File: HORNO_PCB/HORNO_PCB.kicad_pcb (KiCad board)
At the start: 2 copper layers, 198 x 218 mm, 115 parts, among them J0_1 Alimentacion dispositivo seri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, J0_10 Terminales de tornillo espaci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, J0_11 Terminales de tornillo espaci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, J0_12 Terminales de tornillo espaci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, J0_13 Terminales de tornillo espaci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, J0_14 Terminales de tornillo espaci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, J0_15 Terminales de tornillo espaci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, J0_18 Terminales de tornillo espaci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, J0_2 Terminales de tornillo espaci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, J0_3 Terminales de tornillo espaci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, J0_4 Terminales de tornillo espaci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, J0_5 Terminales de tornillo espaci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, J0_6 Terminales de tornillo espaci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, J0_7 Terminales de tornillo espaci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, J0_8 Terminales de tornillo espaci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, J0_9 Terminales de tornillo espaci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, J1 +5V +24V, J10 switch, J11 switch, J12 switch, J13 switch, J14 switch, J15 switch, J16 switch, J17 switch, J18 switch, J19 switch, J20 switch, J21 switch, J22 switch, J23 switch, J24 Screw_Terminal_01x20, J25 Screw_Terminal_01x20, J26 Screw_Terminal_01x20, J27 Screw_Terminal_01x20, J7 24VDC, J8 switch, J9 switch, K1 Relay 1, K2 Relay 2, K6 Relay 4, K7 Relay 3, K8 Relay 2, K9 Relay 1, Q1 2N2222, Q2 2N2222, Q6 IRG4PF50W, Q7 IRG4PF50W, U1 TLP521-1, U10 LM741, U15 TLP250, U17 LM741, U18 LM741, U19 TLP250, U2 TLP521-1, U25 UDN2981A, U3 TLP521-1, U4 TLP521-1, U9 LM741

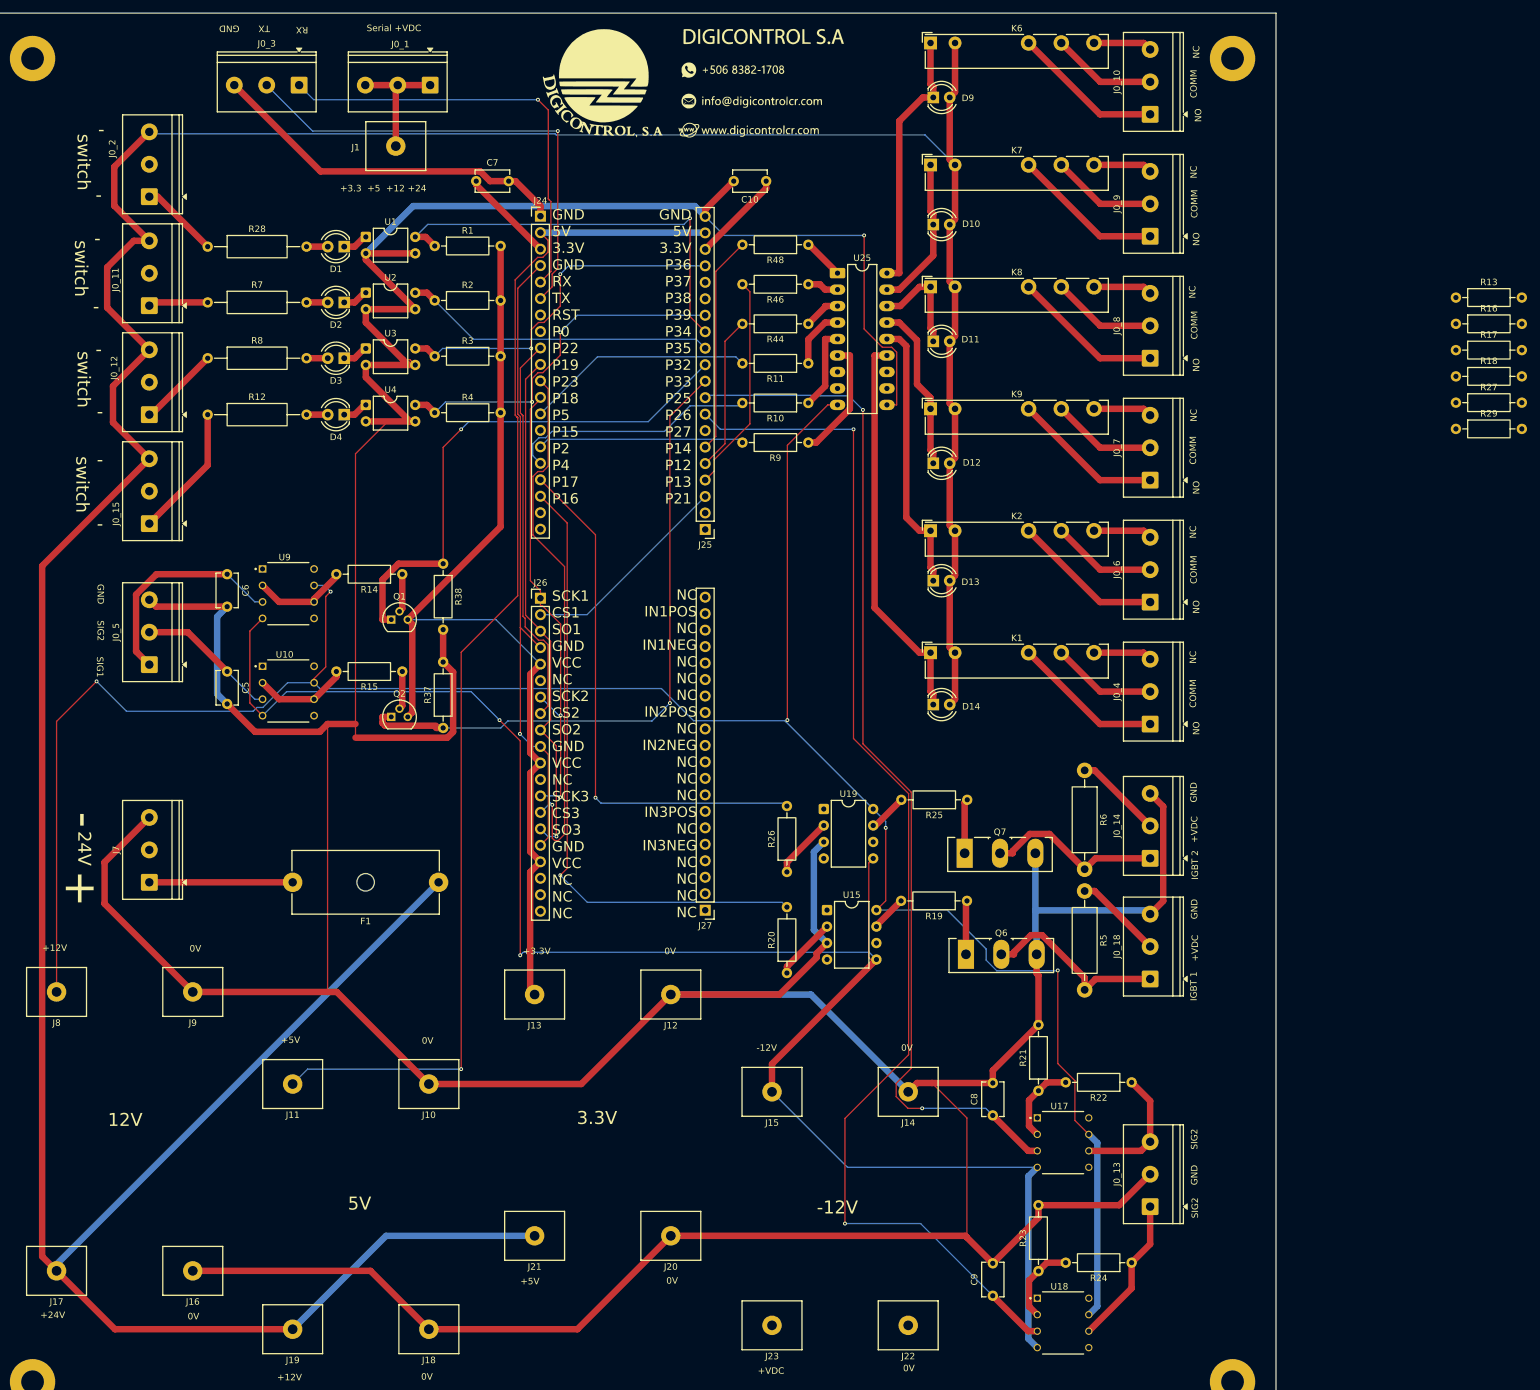
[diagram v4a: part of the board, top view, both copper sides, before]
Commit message: Correccion de esquematico y PCB
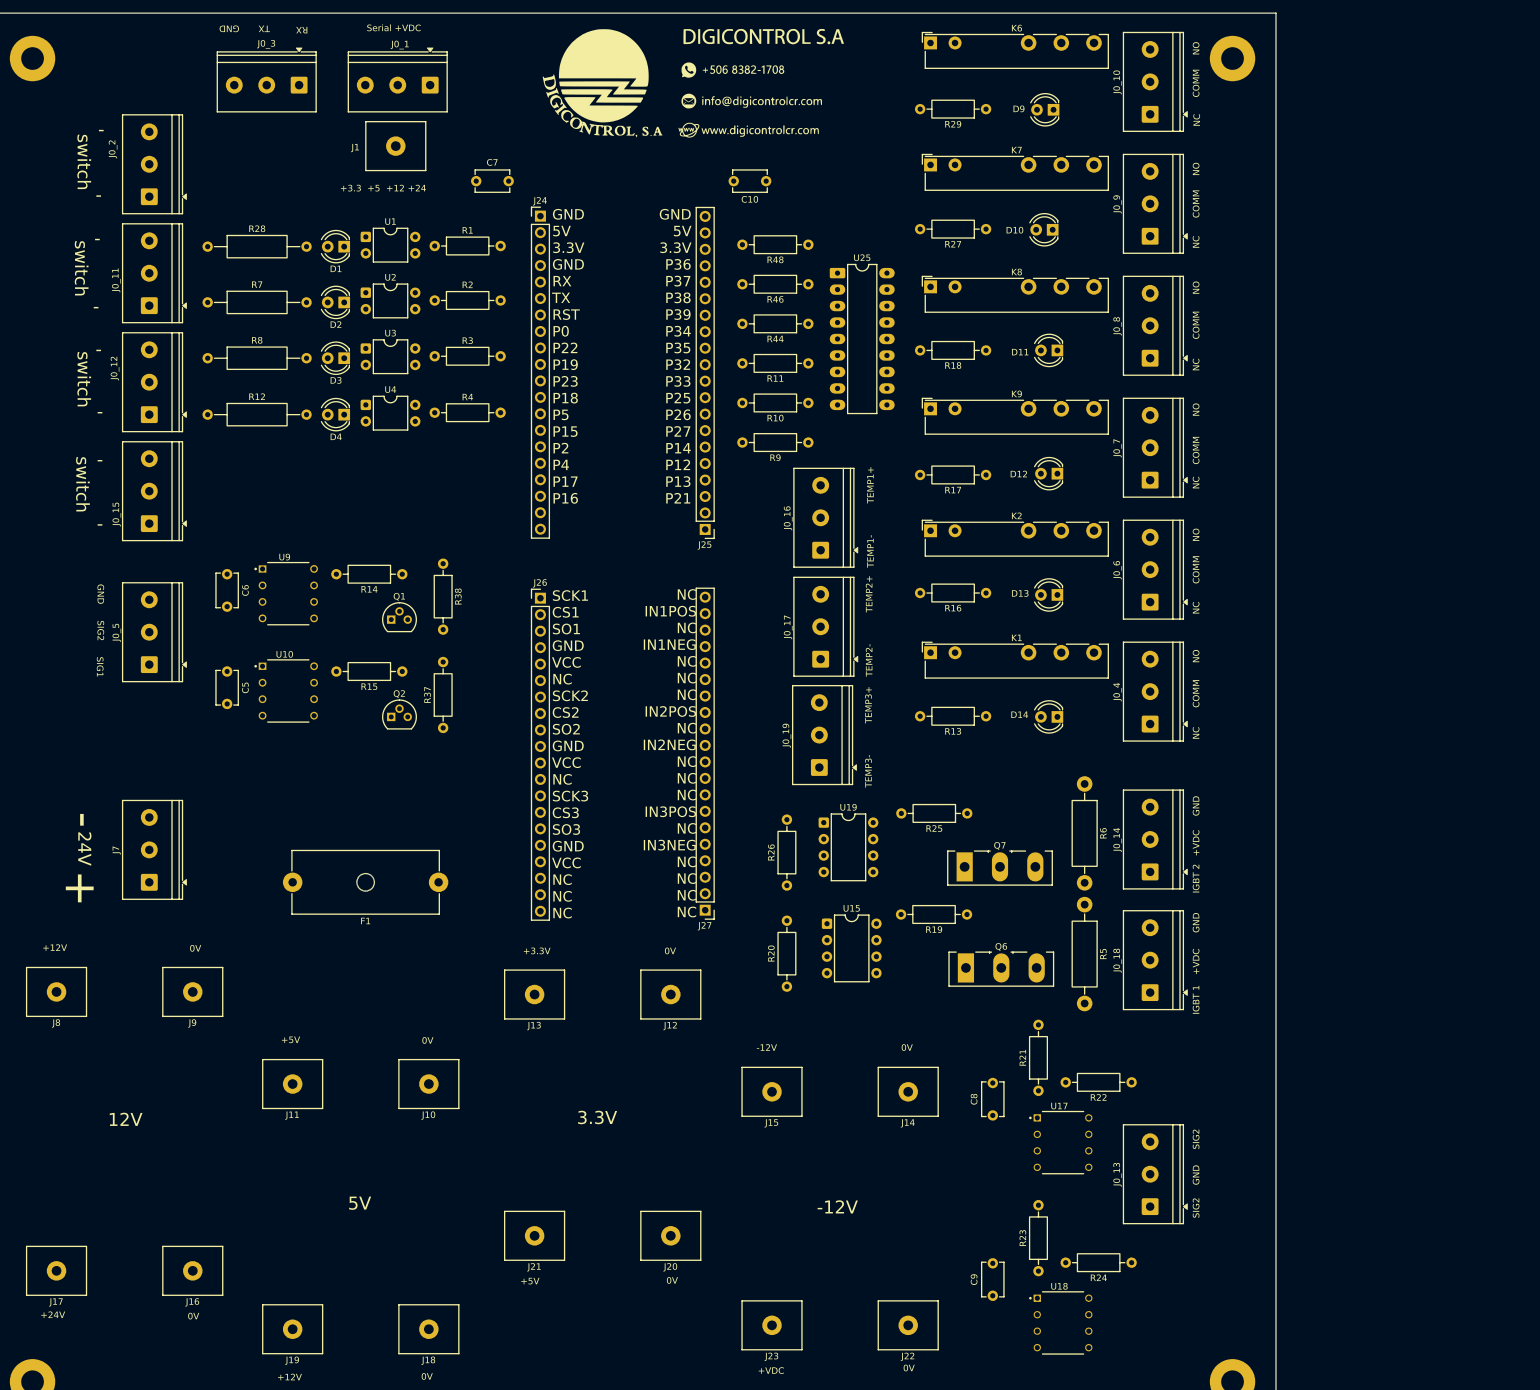
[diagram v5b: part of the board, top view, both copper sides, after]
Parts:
- added J0_16: Terminales de tornillo espaciados en 5mm, TerminalBlock_Phoenix:TerminalBlock_Phoenix_PT-1,5-3-5.0-H_1x03_P5.00mm_Horizontal, F.Cu at (429.5, 249.8)
- added J0_17: Terminales de tornillo espaciados en 5mm, TerminalBlock_Phoenix:TerminalBlock_Phoenix_PT-1,5-3-5.0-H_1x03_P5.00mm_Horizontal, F.Cu at (429.5, 266.6)
- added J0_19: Terminales de tornillo espaciados en 5mm, TerminalBlock_Phoenix:TerminalBlock_Phoenix_PT-1,5-3-5.0-H_1x03_P5.00mm_Horizontal, F.Cu at (429.3, 283.3)
- moved R13 97.0 mm to (455.0, 275.4), turned to 180 degrees
- moved R29 87.6 mm to (455.0, 181.8), turned to 180 degrees
- moved R16 83.5 mm to (455.0, 256.4), turned to 180 degrees
- moved R27 77.2 mm to (455.0, 200.3), turned to 180 degrees
- moved R17 75.0 mm to (455.0, 238.2), turned to 180 degrees
- moved R18 72.6 mm to (455.0, 219.0), turned to 180 degrees
- moved D13 19.3 mm to (466.0, 256.7), turned to 180 degrees
- moved D14 19.2 mm to (466.0, 275.5), turned to 180 degrees
- moved D12 19.2 mm to (466.0, 238.0), turned to 180 degrees
- moved D11 19.2 mm to (466.0, 219.0), turned to 180 degrees
- moved D9 18.6 mm to (465.4, 181.9), turned to 180 degrees
- moved D10 18.4 mm to (465.3, 200.4), turned to 180 degrees
- moved J0_18 2.10 mm to (480.3, 318.0)
- moved Q7 2.10 mm to (451.7, 298.6)
- moved R25 2.10 mm to (452.1, 290.4)
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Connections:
- J27 pad 11: unconnected-(J27-Pin_11-Pad11) -> Net-(J0_17-Pin_1)
- J27 pad 13: unconnected-(J27-Pin_13-Pad13) -> Net-(J0_17-Pin_3)
- J27 pad 17: unconnected-(J27-Pin_17-Pad17) -> Net-(J0_16-Pin_1)
- J27 pad 19: unconnected-(J27-Pin_19-Pad19) -> Net-(J0_16-Pin_3)
- J27 pad 5: unconnected-(J27-Pin_5-Pad5) -> Net-(J0_19-Pin_1)
- J27 pad 7: unconnected-(J27-Pin_7-Pad7) -> Net-(J0_19-Pin_3)
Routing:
- net Net-(D10-K): track 1061.4 -> 0.00 mm, vias 1 -> 0
- net Net-(D10-A): track 599.0 -> 0.00 mm
- net Net-(J8-Pin_1): track 359.0 -> 0.00 mm, vias 5 -> 0
- net Net-(J15-Pin_1): track 268.0 -> 0.00 mm, vias 2 -> 0
- net Net-(J25-Pin_8): track 190.4 -> 0.00 mm, vias 2 -> 0
- net Net-(J11-Pin_1): track 188.4 -> 0.00 mm, vias 1 -> 0
- net Net-(J25-Pin_9): track 160.5 -> 0.00 mm, vias 2 -> 0
- net Net-(J13-Pin_1): track 156.9 -> 0.00 mm
- net Net-(J25-Pin_10): track 100.6 -> 0.00 mm, vias 1 -> 0
- net Net-(J24-Pin_4): track 98.4 -> 0.00 mm, vias 1 -> 0
- net Net-(J24-Pin_18): track 97.6 -> 0.00 mm, vias 1 -> 0
- net Net-(J24-Pin_11): track 84.0 -> 0.00 mm, vias 1 -> 0
- net Net-(J24-Pin_17): track 82.6 -> 0.00 mm, vias 1 -> 0
- net Net-(J25-Pin_11): track 81.5 -> 0.00 mm, vias 1 -> 0
- net Net-(J24-Pin_10): track 79.9 -> 0.00 mm, vias 1 -> 0
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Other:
- board text added: "TEMP1+"
- board text added: "TEMP1-"
- board text added: "TEMP2+"
- board text added: "TEMP2-"
- board text added: "TEMP3+"
- board text added: "TEMP3-"

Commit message: PCB corregida
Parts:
- removed J10, J11, J12, J13, J14, J15, J16, J17, J18, J19, J20, J21, J22, J23, J8, J9: switch, TerminalBlock_MetzConnect:TerminalBlock_MetzConnect_360271_1x01_Horizontal_ScrewM3.0_Boxed
- removed K6: Relay 4, Relay_THT:Relay_SPDT_Fujitsu_FTR-LYCA005x_FormC_Vertical
- added Fuente_1: 12VDC, Fuente_step:step_source, F.Cu at (323.7, 340.0)
- added Fuente_2: 5VDC, Fuente_step:step_source, F.Cu at (360.2, 353.0)
- added Fuente_3: 3.3VDC, Fuente_step:step_source, F.Cu at (397.6, 340.0)
- added Fuente_4: -12VDC, Fuente_step:step_source, F.Cu at (436.5, 353.0)
- moved C8 7.87 mm to (455.7, 344.8)
- moved C9 6.80 mm to (456.0, 371.5)
- moved R21 6.00 mm to (458.1, 336.5)
- moved U15 5.62 mm to (430.5, 313.0)
- moved R23 5.48 mm to (458.1, 363.2)
- moved R20 5.42 mm to (424.3, 322.5)
- moved R19 5.04 mm to (452.1, 311.0)
- moved Q6 3.80 mm to (451.9, 318.0)
- moved J0_14 2.40 mm to (480.3, 297.0)
- moved R5 2.06 mm to (470.2, 306.5)
- moved Q7 1.62 mm to (451.7, 297.0)
- moved R22 1.16 mm to (477.4, 333.0)
- moved U17 1.06 mm to (466.8, 342.2)
- moved J0_13 1.00 mm to (480.3, 352.0)
- moved R25 0.38 mm to (452.1, 290.0)
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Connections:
- J0_10 pad 2: Net-(J0_10-Pin_2) -> unconnected-(J0_10-Pin_2-Pad2)
- J0_10 pad 3: Net-(J0_10-Pin_3) -> Net-(D10-K)
- R29 pad 2: Net-(U25-O1) -> Net-(J0_10-Pin_1)
- R48 pad 1: Net-(U25-I1) -> Net-(J0_10-Pin_1)
- U25 pad 1: Net-(U25-I1) -> unconnected-(U25-I1-Pad1)
- U25 pad 18: Net-(U25-O1) -> unconnected-(U25-O1-Pad18)
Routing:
- net Net-(D10-K): track 0.00 -> 1046.3 mm
- net Net-(Fuente_1-OUT+): track 0.00 -> 364.9 mm, vias 0 -> 5
- net Net-(Fuente_1-IN+): track 0.00 -> 326.0 mm
- net Net-(Fuente_4-OUT+): track 0.00 -> 232.0 mm, vias 0 -> 1
- net Net-(Fuente_2-OUT+): track 0.00 -> 190.2 mm, vias 0 -> 1
- net Net-(J25-Pin_8): track 0.00 -> 185.1 mm, vias 0 -> 1
- net Net-(Fuente_3-OUT+): track 0.00 -> 172.0 mm, vias 0 -> 1
- net Net-(J25-Pin_9): track 0.00 -> 161.7 mm, vias 0 -> 1
- net Net-(J24-Pin_18): track 0.00 -> 103.8 mm, vias 0 -> 1
- net Net-(J25-Pin_10): track 0.00 -> 99.4 mm, vias 0 -> 1
- net Net-(J24-Pin_4): track 0.00 -> 97.1 mm
- net Net-(J24-Pin_17): track 0.00 -> 86.9 mm, vias 0 -> 1
- net Net-(J25-Pin_11): track 0.00 -> 79.3 mm, vias 0 -> 1
- net Net-(J24-Pin_10): track 0.00 -> 77.3 mm
- net Net-(J0_3-Pin_2): track 0.00 -> 71.6 mm, vias 0 -> 1
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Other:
- board text added: "+VDC / 0V"
- board text added: "0V / +VDC"
- board text added: "3.3 VDC"

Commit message: Alimentacion de 24V para el UDN y cambiar rele de salida para conectar un SSR
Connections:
- R48 pad 1: Net-(J0_10-Pin_1) -> Net-(U25-I1)
- U25 pad 1: unconnected-(U25-I1-Pad1) -> Net-(U25-I1)
- U25 pad 18: unconnected-(U25-O1-Pad18) -> Net-(J0_10-Pin_1)
- U25 pad 9: Net-(Fuente_1-OUT+) -> Net-(Fuente_1-IN+)
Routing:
- net Net-(Fuente_1-IN+): track 326.0 -> 456.4 mm, vias 0 -> 1
- net Net-(Fuente_1-OUT+): track 364.9 -> 335.7 mm
- net Net-(D10-K): track 1046.3 -> 1069.0 mm
- net Net-(U25-I1): track 0.00 -> 6.55 mm
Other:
- board text added: "0 V"

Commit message: PCB corregida
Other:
- board text added: "24 VDC"
- board text removed: "3.3 VDC"
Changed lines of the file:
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@@
 		)
 	)
-	(gr_text "3.3 VDC"
+	(gr_text "24 VDC"
 		(at 488 186 90)
 		(layer "F.SilkS")
